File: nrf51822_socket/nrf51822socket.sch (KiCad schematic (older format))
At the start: 14 parts, among them J1 Teste analógico, J2 Esquerdo, J3 Direito, J4 Enable LDO, J5 Input Output, Q1 Q_NMOS_GSD, U1 LN1134

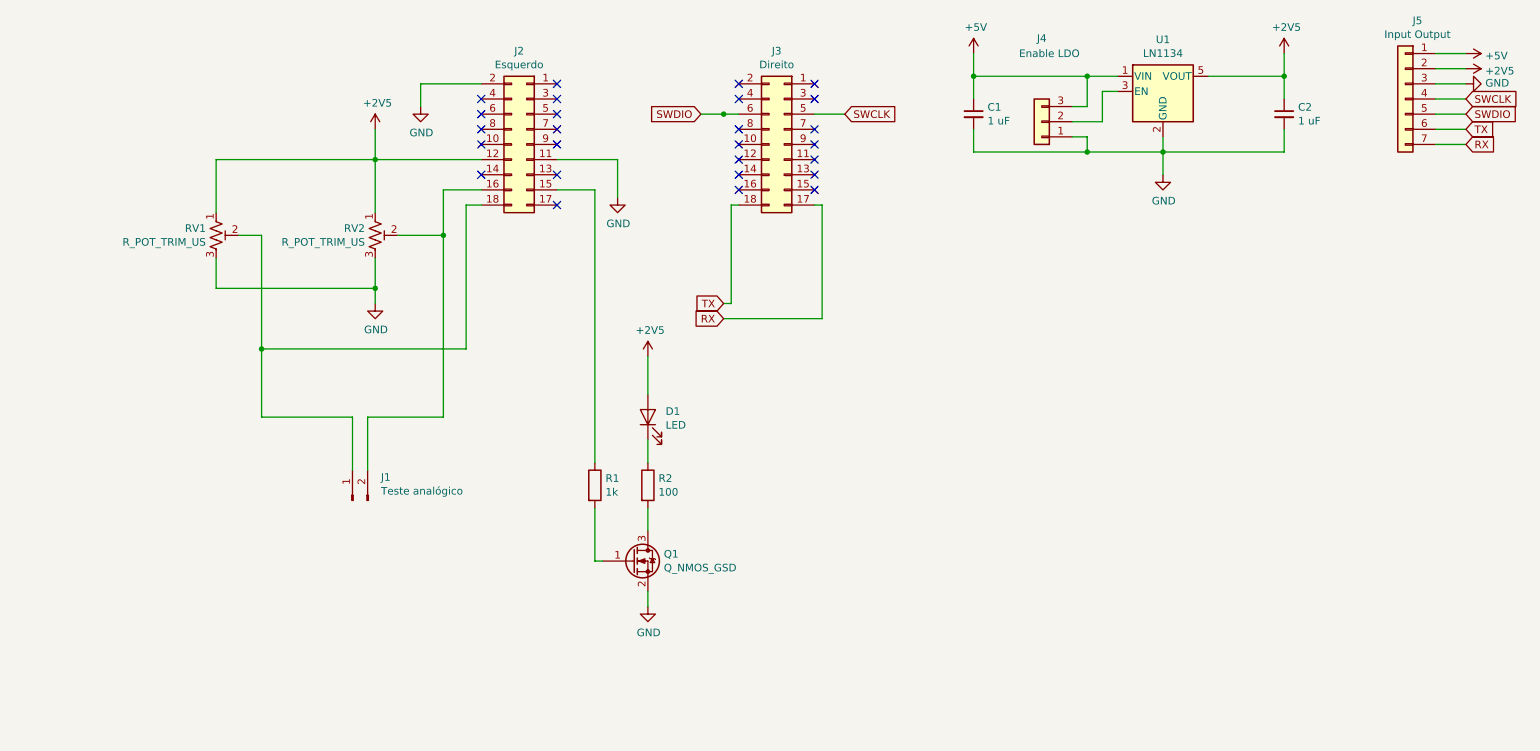
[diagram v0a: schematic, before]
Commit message: V 0.2 do socket NRF51822 - esquematico e layout
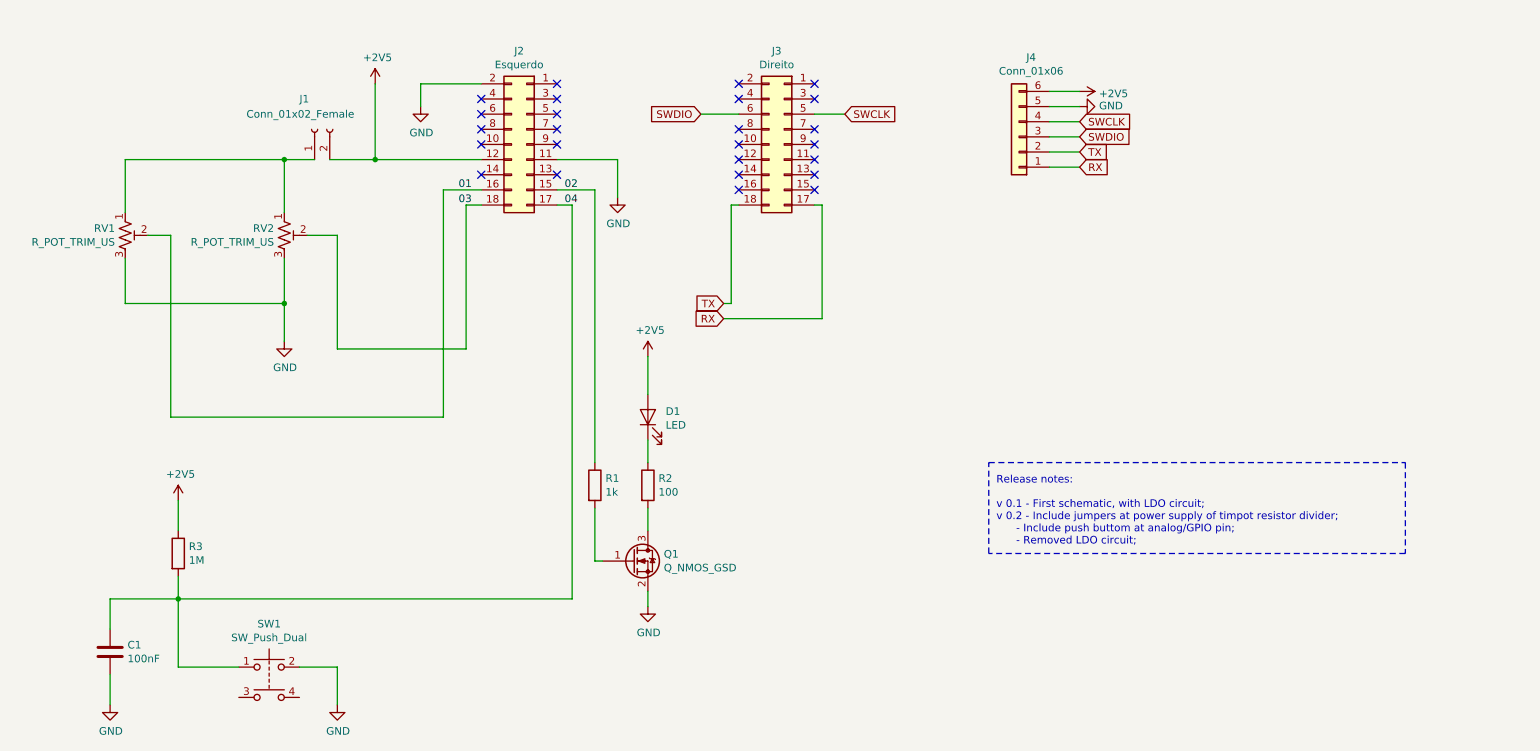
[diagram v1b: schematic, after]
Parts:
- removed C1, C2: 1 uF, Capacitor_THT:CP_Radial_D6.3mm_P2.50mm, symbol Device:C_Small
- removed J1: Teste analógico, Connector_PinHeader_2.54mm:PinHeader_1x02_P2.54mm_Vertical, symbol Connector:Conn_01x02_Male
- removed J4: Enable LDO, Connector_PinSocket_2.54mm:PinSocket_1x03_P2.54mm_Vertical, symbol Connector_Generic:Conn_01x03
- removed J5: Input Output, Connector_PinSocket_2.54mm:PinSocket_1x07_P2.54mm_Vertical, symbol Connector_Generic:Conn_01x07
- removed U1: LN1134, Package_TO_SOT_SMD:SOT-23-5, symbol Regulator_Linear:AP2112K-1.8
- added C1: 100nF, Capacitor_THT:CP_Radial_D5.0mm_P2.50mm, symbol Device:C
- added J1: Conn_01x02_Female, Connector_PinSocket_2.54mm:PinSocket_1x02_P2.54mm_Vertical, symbol Connector:Conn_01x02_Female
- added J4: Conn_01x06, Connector_PinSocket_2.54mm:PinSocket_1x06_P2.54mm_Vertical, symbol Connector_Generic:Conn_01x06
- added R3: 1M, Resistor_THT:R_Axial_DIN0207_L6.3mm_D2.5mm_P7.62mm_Horizontal, symbol Device:R
- added SW1: SW_Push_Dual, Button_Switch_THT:SW_TH_Tactile_Omron_B3F-10xx, symbol Switch:SW_Push_Dual
- R1, R2: footprint Resistor_SMD:R_0805_2012Metric_Pad1.15x1.40mm_HandSolder -> Resistor_THT:R_Axial_DIN0207_L6.3mm_D2.5mm_P7.62mm_Horizontal
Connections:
- net +2V5: now also J1.2 (Pin_2), J4.6 (Pin_6), R3.1; no longer RV1.1, RV2.1
- net GND: now also C1.2, J4.5 (Pin_5), SW1.2
- net RX: now also J4.1 (Pin_1)
- net SWCLK: now also J4.4 (Pin_4)
- net SWDIO: now also J4.3 (Pin_3)
- net TX: now also J4.2 (Pin_2)
- net 02: now reaches J2.15 (Pin_15), R1.1
- net at RV2.2: now also J2.18 (Pin_18); no longer J2.16 (Pin_16)
- net 04: now reaches J2.17 (Pin_17)
- net 04: now also C1.1, R3.2, SW1.1
- net 01: now reaches RV1.2
- net 01: now also J2.16 (Pin_16); no longer J2.18 (Pin_18)
- new net: J1.1 (Pin_1), RV1.1, RV2.1
- no-connect marks 26 -> 25
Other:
- note added: "Release notes:\n\nv 0.1 - First schematic, with LDO circuit;\nv 0.2 - Include jumpers at power supply of timpot resistor divider;\n - Include push buttom at analog/GPIO pin;\n - Removed LDO circuit; \n"
- moved on the sheet: RV1, RV2

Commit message: algumas melhorias
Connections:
- net GND: now also SW1.4; no longer SW1.2
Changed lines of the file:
@@
 $EndComp
-Wire Wire Line
-	2350 6100 2600 6100
-Wire Wire Line
-	2600 6100 2600 6350
 Wire Wire Line
 	1550 5500 1550 5650
@@
 Wire Wire Line
 	1500 3250 1500 4450
+Wire Wire Line
+	2350 6300 2600 6300
+Wire Wire Line
+	2600 6300 2600 6350
 $EndSCHEMATC

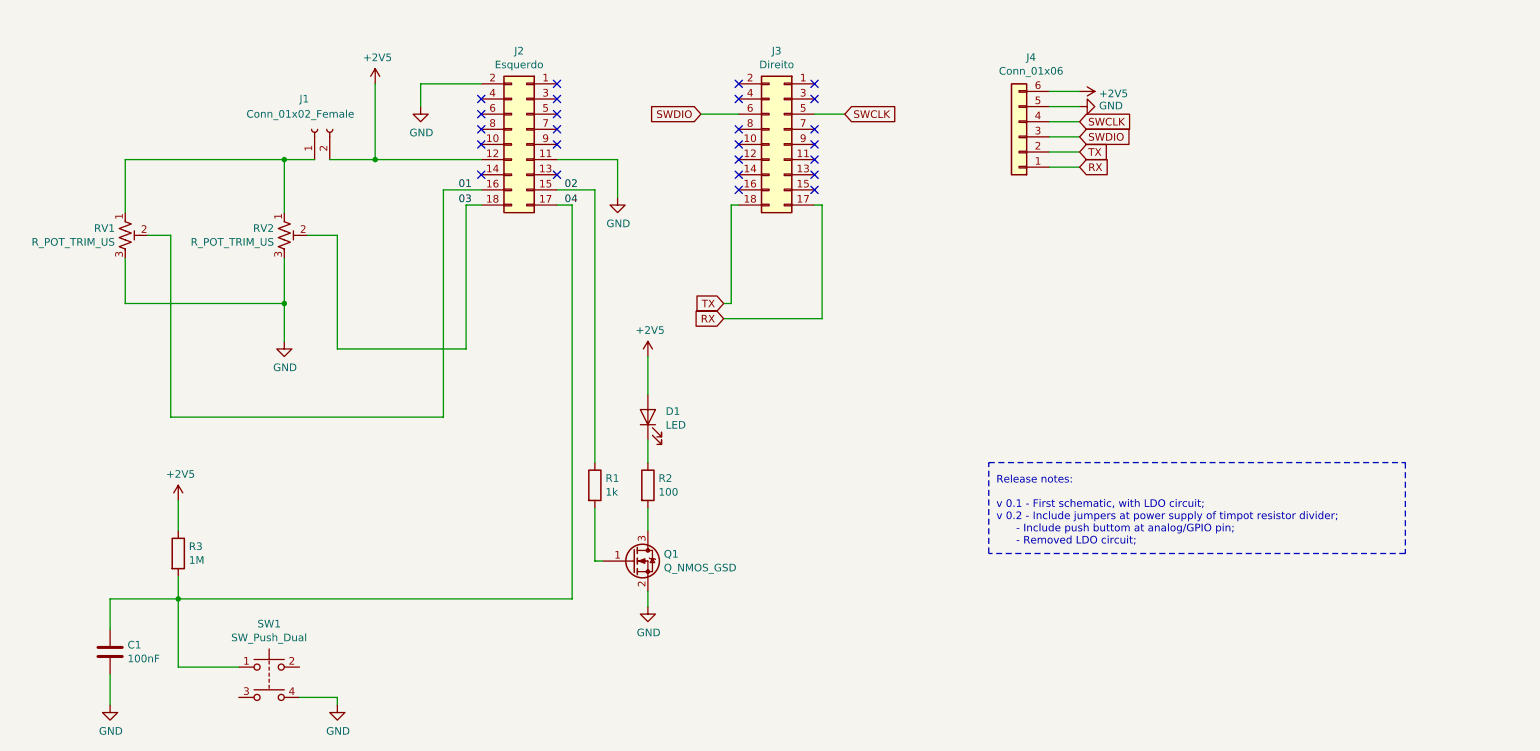
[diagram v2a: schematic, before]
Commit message: modificando disposição no esquemático, mas não o esquemático em si
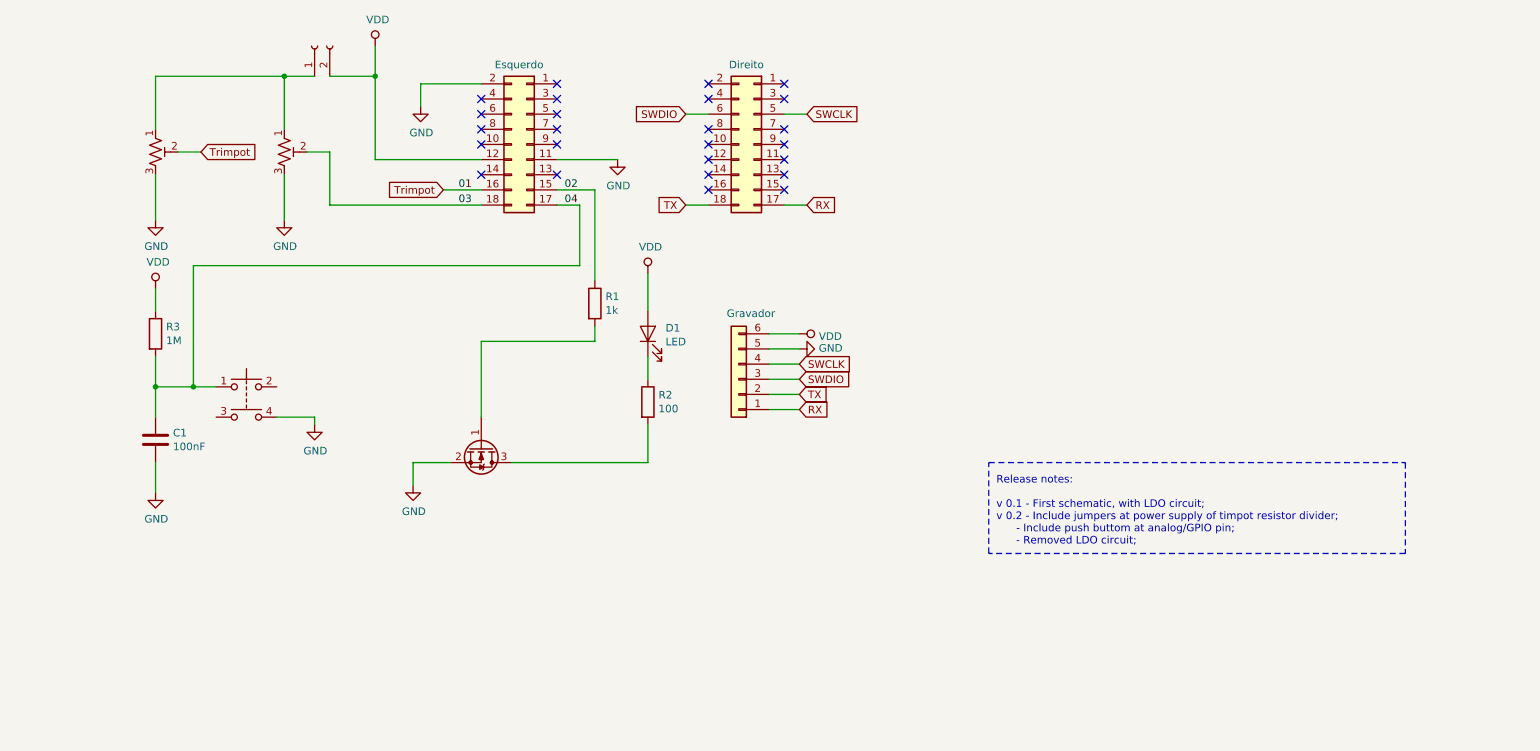
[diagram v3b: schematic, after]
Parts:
- J4: value Conn_01x06 -> Gravador
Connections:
- net 03: now also J2.18 (Pin_18), RV2.2
- net +2V5 renamed VDD
- net 01 renamed Trimpot
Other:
- moved on the sheet: C1, D1, R1, R2, R3
